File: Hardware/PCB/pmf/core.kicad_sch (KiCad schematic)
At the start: 39 parts, among them U1 AS3320, U2 TL072

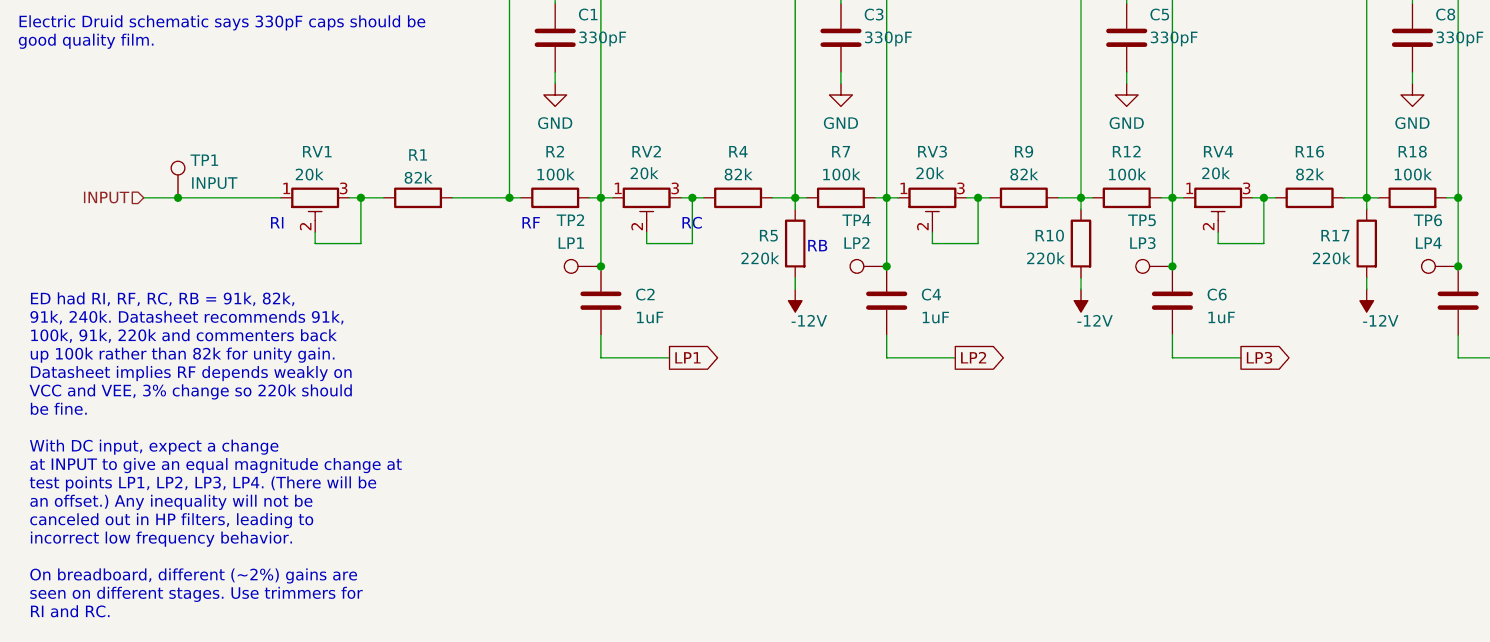
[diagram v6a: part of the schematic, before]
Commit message: Bigger trimmers for RC; slightly move expansion header
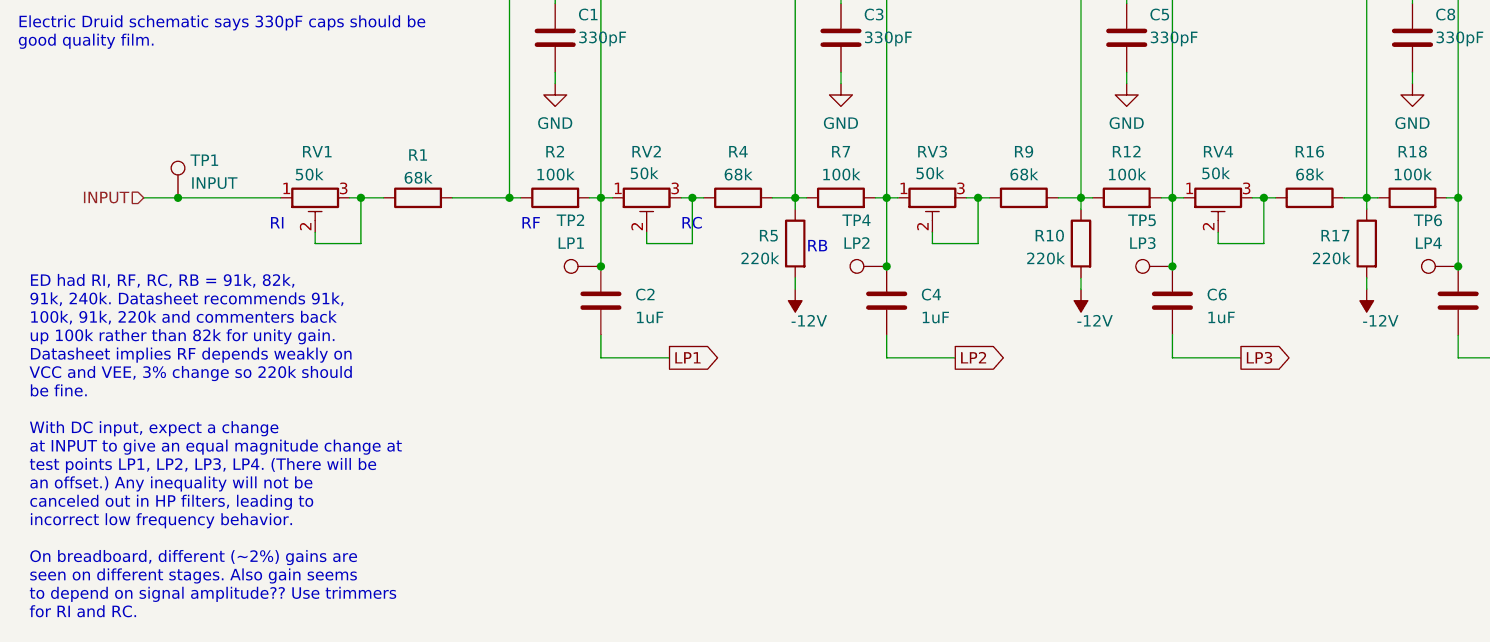
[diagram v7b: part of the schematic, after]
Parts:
- R1, R16, R4, R9: value 82k -> 68k
- RV1, RV2, RV3, RV4: value 20k -> 50k
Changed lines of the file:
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@@
     (effects (font (size 1.27 1.27)) (justify left bottom))
   )
-  (text "ED had RI, RF, RC, RB = 91k, 82k, \n91k, 240k. Datasheet recommends 91k, \n100k, 91k, 220k and commenters back \nup 100k rather than 82k for unity gain.\nDatasheet implies RF depends weakly on \nVCC and VEE, 3% change so 220k should \nbe fine.\n\nWith DC input, expect a change\nat INPUT to give an equal magnitude change at \ntest points LP1, LP2, LP3, LP4. (There will be \nan offset.) Any inequality will not be \ncanceled out in HP filters, leading to\nincorrect low frequency behavior.\n\nOn breadboard, different (~2%) gains are\nseen on different stages. Use trimmers for\nRI and RC."
+  (text "ED had RI, RF, RC, RB = 91k, 82k, \n91k, 240k. Datasheet recommends 91k, \n100k, 91k, 220k and commenters back \nup 100k rather than 82k for unity gain.\nDatasheet implies RF depends weakly on \nVCC and VEE, 3% change so 220k should \nbe fine.\n\nWith DC input, expect a change\nat INPUT to give an equal magnitude change at \ntest points LP1, LP2, LP3, LP4. (There will be \nan offset.) Any inequality will not be \ncanceled out in HP filters, leading to\nincorrect low frequency behavior.\n\nOn breadboard, different (~2%) gains are\nseen on different stages. Also gain seems\nto depend on signal amplitude?? Use trimmers \nfor RI and RC."
     (at 55.88 165.1 0)
     (effects (font (size 1.27 1.27)) (justify left bottom))
@@
       (effects (font (size 1.27 1.27)))
     )
-    (property "Value" "82k" (at 166.37 115.57 90)
+    (property "Value" "68k" (at 166.37 115.57 90)
       (effects (font (size 1.27 1.27)))
     )
@@
       (effects (font (size 1.27 1.27)))
     )
-    (property "Value" "82k" (at 198.12 115.57 90)
+    (property "Value" "68k" (at 198.12 115.57 90)
       (effects (font (size 1.27 1.27)))
     )
@@
       (effects (font (size 1.27 1.27)))
     )
-    (property "Value" "82k" (at 134.62 115.57 90)
+    (property "Value" "68k" (at 134.62 115.57 90)
       (effects (font (size 1.27 1.27)))
     )
@@
       (effects (font (size 1.27 1.27)))
     )
-    (property "Value" "20k" (at 186.055 115.443 90)
+    (property "Value" "50k" (at 186.055 115.443 90)
       (effects (font (size 1.27 1.27)) (justify right))
     )
@@
       (effects (font (size 1.27 1.27)))
     )
-    (property "Value" "20k" (at 122.555 115.443 90)
+    (property "Value" "50k" (at 122.555 115.443 90)
       (effects (font (size 1.27 1.27)) (justify right))
     )
@@
       (effects (font (size 1.27 1.27)))
     )
-    (property "Value" "82k" (at 99.06 115.9311 90)
+    (property "Value" "68k" (at 99.06 115.9311 90)
       (effects (font (size 1.27 1.27)))
     )
@@
       (effects (font (size 1.27 1.27)))
     )
-    (property "Value" "20k" (at 154.305 115.443 90)
+    (property "Value" "50k" (at 154.305 115.443 90)
       (effects (font (size 1.27 1.27)) (justify right))
     )
@@
       (effects (font (size 1.27 1.27)) (justify right))
     )
-    (property "Value" "20k" (at 85.344 115.57 90)
+    (property "Value" "50k" (at 85.344 115.57 90)
       (effects (font (size 1.27 1.27)) (justify right))
     )

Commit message: Hardware symbols test
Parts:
- C1, C3, C5, C8: footprint AO_tht:C_Rect_L7.2mm_W2.5mm_P5.00mm_FKS2_FKP2_MKS2_MKP2 -> AO_tht:C_Disc_D3.0mm_W1.6mm_P2.50mm
- C2, C4, C6, C7, C9: footprint AO_tht:C_Rect_L7.2mm_W7.2mm_P5.00mm_FKS2_FKP2_MKS2_MKP2 -> AO_tht:C_Disc_D3.0mm_W1.6mm_P2.50mm
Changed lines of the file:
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@@
       (effects (font (size 1.27 1.27)) (justify left))
     )
-    (property "Footprint" "AO_tht:C_Rect_L7.2mm_W2.5mm_P5.00mm_FKS2_FKP2_MKS2_MKP2" (at 178.7652 104.14 0)
+    (property "Footprint" "AO_tht:C_Disc_D3.0mm_W1.6mm_P2.50mm" (at 178.7652 104.14 0)
       (effects (font (size 1.27 1.27)) hide)
     )
@@
       (effects (font (size 1.27 1.27)) (justify left))
     )
-    (property "Footprint" "AO_tht:C_Rect_L7.2mm_W7.2mm_P5.00mm_FKS2_FKP2_MKS2_MKP2" (at 215.5952 133.35 0)
+    (property "Footprint" "AO_tht:C_Disc_D3.0mm_W1.6mm_P2.50mm" (at 215.5952 133.35 0)
       (effects (font (size 1.27 1.27)) hide)
     )
@@
       (effects (font (size 1.27 1.27)) (justify left))
     )
-    (property "Footprint" "AO_tht:C_Rect_L7.2mm_W7.2mm_P5.00mm_FKS2_FKP2_MKS2_MKP2" (at 120.3452 133.35 0)
+    (property "Footprint" "AO_tht:C_Disc_D3.0mm_W1.6mm_P2.50mm" (at 120.3452 133.35 0)
       (effects (font (size 1.27 1.27)) hide)
     )
@@
       (effects (font (size 1.27 1.27)) (justify left))
     )
-    (property "Footprint" "AO_tht:C_Rect_L7.2mm_W7.2mm_P5.00mm_FKS2_FKP2_MKS2_MKP2" (at 183.8452 133.35 0)
+    (property "Footprint" "AO_tht:C_Disc_D3.0mm_W1.6mm_P2.50mm" (at 183.8452 133.35 0)
       (effects (font (size 1.27 1.27)) hide)
     )
@@
       (effects (font (size 1.27 1.27)) (justify left))
     )
-    (property "Footprint" "AO_tht:C_Rect_L7.2mm_W2.5mm_P5.00mm_FKS2_FKP2_MKS2_MKP2" (at 210.5152 104.14 0)
+    (property "Footprint" "AO_tht:C_Disc_D3.0mm_W1.6mm_P2.50mm" (at 210.5152 104.14 0)
       (effects (font (size 1.27 1.27)) hide)
     )
@@
       (effects (font (size 1.27 1.27)))
     )
-    (property "Footprint" "AO_tht:C_Rect_L7.2mm_W7.2mm_P5.00mm_FKS2_FKP2_MKS2_MKP2" (at 205.74 56.1848 0)
+    (property "Footprint" "AO_tht:C_Disc_D3.0mm_W1.6mm_P2.50mm" (at 205.74 56.1848 0)
       (effects (font (size 1.27 1.27)) hide)
     )
@@
       (effects (font (size 1.27 1.27)) (justify left))
     )
-    (property "Footprint" "AO_tht:C_Rect_L7.2mm_W2.5mm_P5.00mm_FKS2_FKP2_MKS2_MKP2" (at 147.0152 104.14 0)
+    (property "Footprint" "AO_tht:C_Disc_D3.0mm_W1.6mm_P2.50mm" (at 147.0152 104.14 0)
       (effects (font (size 1.27 1.27)) hide)
     )
@@
       (effects (font (size 1.27 1.27)) (justify left))
     )
-    (property "Footprint" "AO_tht:C_Rect_L7.2mm_W7.2mm_P5.00mm_FKS2_FKP2_MKS2_MKP2" (at 152.0952 133.35 0)
+    (property "Footprint" "AO_tht:C_Disc_D3.0mm_W1.6mm_P2.50mm" (at 152.0952 133.35 0)
       (effects (font (size 1.27 1.27)) hide)
     )
@@
       (effects (font (size 1.27 1.27)) (justify left))
     )
-    (property "Footprint" "AO_tht:C_Rect_L7.2mm_W2.5mm_P5.00mm_FKS2_FKP2_MKS2_MKP2" (at 115.2652 104.14 0)
-      (effects (font (size 1.27 1.27)) hide)
-    )
+    (property "Footprint" "AO_tht:C_Disc_D3.0mm_W1.6mm_P2.50mm" (at 115.2652 104.14 0)
+      (effects (font (size 1.27 1.27)) hide)
+    )
